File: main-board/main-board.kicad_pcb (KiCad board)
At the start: 2 copper layers, 26 parts, among them IC1 ATMEGA328-A, IC2 FT232RL, J1 INTERFACE1, J2 INTERFACE3, J3 INTERFACE5, J4 INTERFACE5, J5 INTERFACE2, J6 INTERFACE4, J7 INTERFACE6, J8 INTERFACE6, P1 USB_B, P2 CONN_01X02, Y1 Crystal

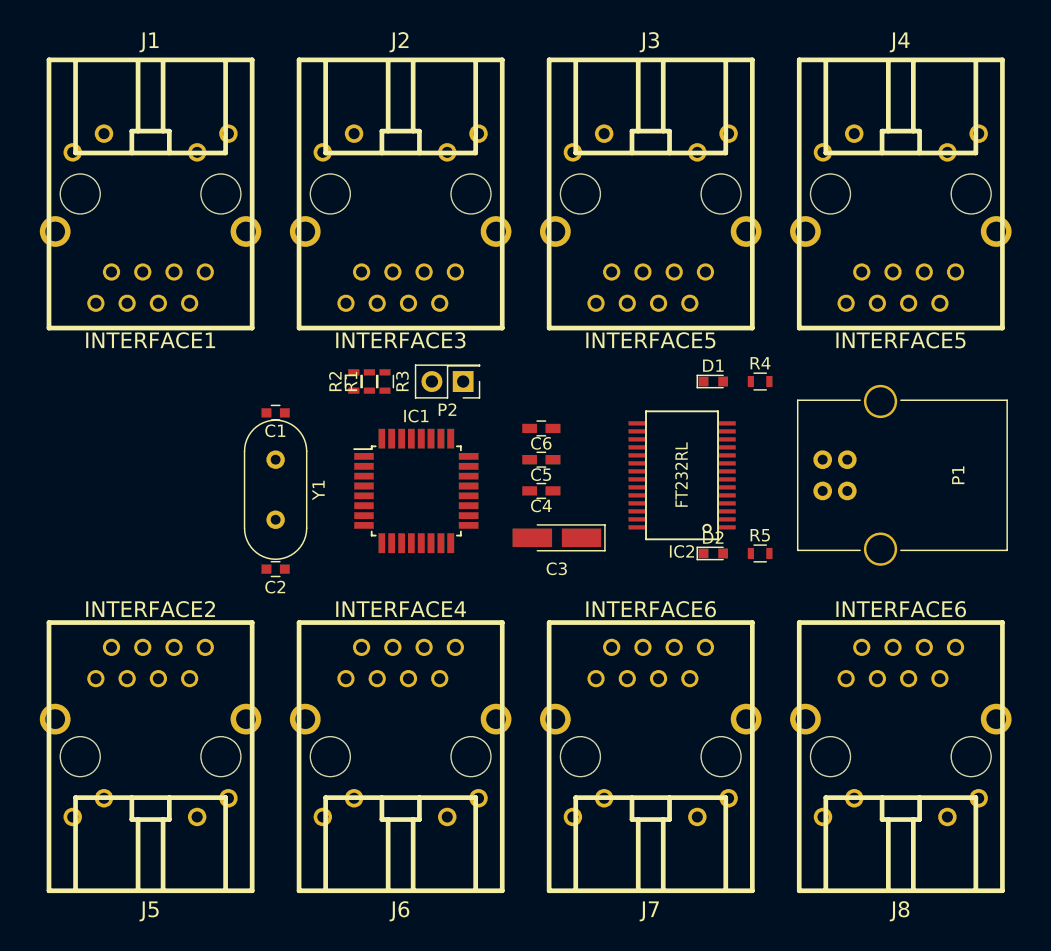
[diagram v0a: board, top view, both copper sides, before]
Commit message: finidhed routing the main-board
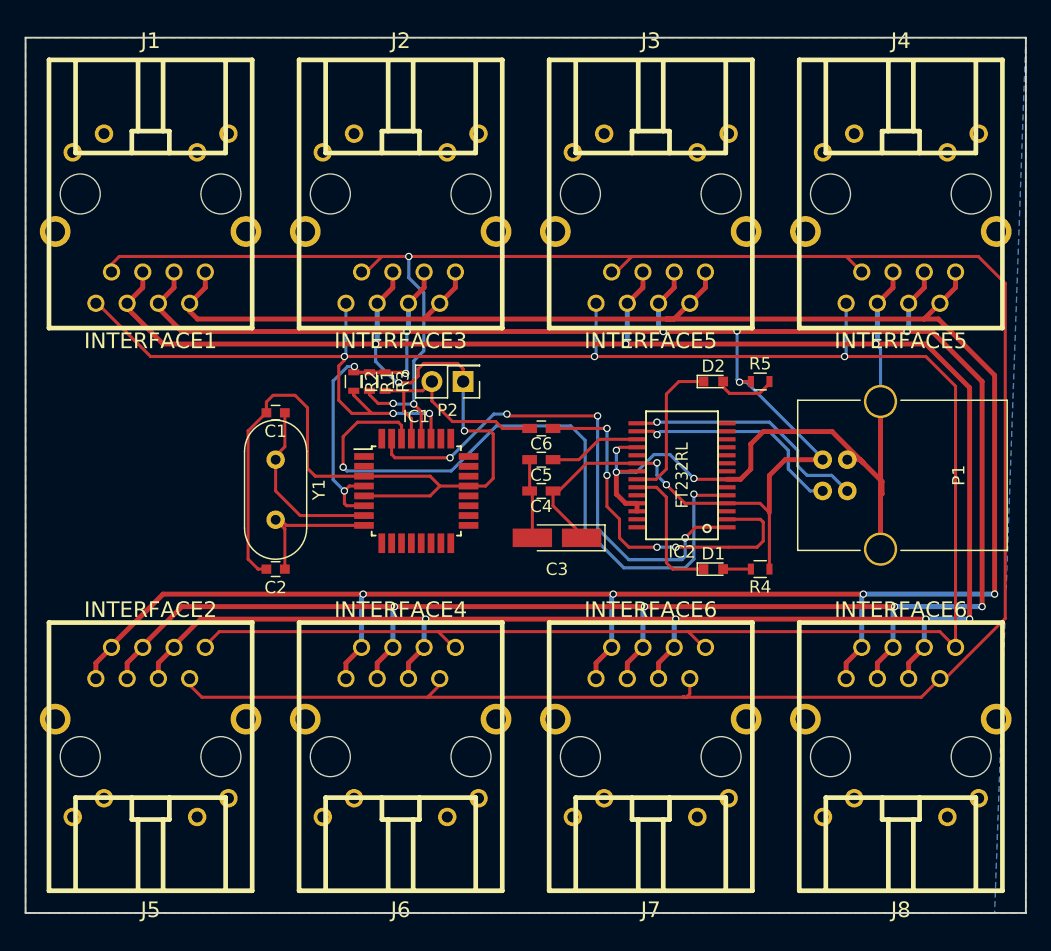
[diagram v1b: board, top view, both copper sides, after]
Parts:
- moved D1 15.2 mm to (124.5, 68.6)
- moved R4 15.2 mm to (128.3, 68.6), turned to 180 degrees
- moved D2 14.0 mm to (124.5, 53.3)
- moved R5 14.0 mm to (128.3, 53.3)
- turned R1 to 270 degrees
- turned R2 to 270 degrees
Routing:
- net GND: track 0.00 -> 322.3 mm, vias 0 -> 12
- net +5V: track 0.00 -> 277.8 mm, vias 0 -> 14
- net +12V: track 0.00 -> 203.3 mm, vias 0 -> 4
- net SCL: track 0.00 -> 201.6 mm, vias 0 -> 3
- net SDA: track 0.00 -> 189.5 mm, vias 0 -> 5
- net RX1: track 0.00 -> 56.3 mm, vias 0 -> 2
- net TX1: track 0.00 -> 42.4 mm, vias 0 -> 4
- net DTR: track 0.00 -> 30.5 mm, vias 0 -> 4
- net Net-(IC2-Pad15): track 0.00 -> 20.2 mm, vias 0 -> 1
- net RST: track 0.00 -> 18.7 mm
- net Net-(IC2-Pad16): track 0.00 -> 18.2 mm, vias 0 -> 1
- net XTAL1: track 0.00 -> 14.7 mm
- net Net-(D2-Pad1): track 0.00 -> 12.3 mm
- net XTAL2: track 0.00 -> 11.7 mm
- net Net-(D1-Pad1): track 0.00 -> 11.3 mm
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- added copper zone on B.Cu, net GND
- added copper zone on F.Cu, net GND
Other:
- board outline added: 81.3 x 71.1 mm

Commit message: final commit with proper silkscreen and pdf exports
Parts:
- renumbered J1 to ?, J2 to ?, J3 to ?, J4 to ?, J5 to ?, J6 to ?, J7 to ?, J8 to ?
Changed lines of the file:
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@@
     (links 108)
     (no_connects 0)
-    (area 68.504999 25.324999 149.935001 96.595001)
+    (area 68.504999 23.93 149.935001 97.6852)
     (thickness 1.6)
     (drawings 4)
@@
     (pad_to_mask_clearance 0.2)
     (aux_axis_origin 0 0)
-    (visible_elements FFFFFF7F)
+    (visible_elements 7FFFFFFF)
     (pcbplotparams
       (layerselection 0x00030_80000001)
@@
       (psnegative false)
       (psa4output false)
-      (plotreference true)
-      (plotvalue true)
+      (plotreference false)
+      (plotvalue false)
       (plotinvisibletext false)
       (padsonsilk false)
@@
       (outputformat 1)
       (mirror false)
-      (drillshape 1)
+      (drillshape 0)
       (scaleselection 1)
-      (outputdirectory ""))
+      (outputdirectory gerbers/))
   )
   (net 0 "")
@@
     (at 78.74 38.1 180)
     (descr "RJ45 + led indicators, Wiznet P/N RB1-125BAG1A")
-    (fp_text reference J1 (at 0 12.446 180) (layer F.SilkS)
+    (fp_text reference "" (at 0 12.446 180) (layer F.SilkS)
       (effects (font (thickness 0.3048)))
     )
@@
     (at 99.06 38.1 180)
     (descr "RJ45 + led indicators, Wiznet P/N RB1-125BAG1A")
-    (fp_text reference J2 (at 0 12.446 180) (layer F.SilkS)
+    (fp_text reference "" (at 0 12.446 180) (layer F.SilkS)
       (effects (font (thickness 0.3048)))
     )
@@
     (at 119.38 38.1 180)
     (descr "RJ45 + led indicators, Wiznet P/N RB1-125BAG1A")
-    (fp_text reference J3 (at 0 12.446 180) (layer F.SilkS)
+    (fp_text reference "" (at 0 12.446 180) (layer F.SilkS)
       (effects (font (thickness 0.3048)))
     )
@@
     (at 139.7 38.1 180)
     (descr "RJ45 + led indicators, Wiznet P/N RB1-125BAG1A")
-    (fp_text reference J4 (at 0 12.446 180) (layer F.SilkS)
+    (fp_text reference "" (at 0 12.446 180) (layer F.SilkS)
       (effects (font (thickness 0.3048)))
     )
@@
     (at 78.74 83.82)
     (descr "RJ45 + led indicators, Wiznet P/N RB1-125BAG1A")
-    (fp_text reference J5 (at 0 12.446) (layer F.SilkS)
+    (fp_text reference "" (at 0 12.446) (layer F.SilkS)
       (effects (font (thickness 0.3048)))
     )
@@
     (at 99.06 83.82)
     (descr "RJ45 + led indicators, Wiznet P/N RB1-125BAG1A")
-    (fp_text reference J6 (at 0 12.446) (layer F.SilkS)
+    (fp_text reference "" (at 0 12.446) (layer F.SilkS)
       (effects (font (thickness 0.3048)))
     )
@@
     (at 119.38 83.82)
     (descr "RJ45 + led indicators, Wiznet P/N RB1-125BAG1A")
-    (fp_text reference J7 (at 0 12.446) (layer F.SilkS)
+    (fp_text reference "" (at 0 12.446) (layer F.SilkS)
       (effects (font (thickness 0.3048)))
     )
@@
     (at 139.7 83.82)
     (descr "RJ45 + led indicators, Wiznet P/N RB1-125BAG1A")
-    (fp_text reference J8 (at 0 12.446) (layer F.SilkS)
-      (effects (font (thickness 0.3048)))
-    )
+    (fp_text reference "" (at 0 12.446) (layer F.SilkS)
+      (effects (font (thickness 0.3048)))
+    )

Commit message: Add branding
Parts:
- added G***: LOGO, custom:logomark.soldermask, F.Cu at (78.1, 64.1)
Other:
- board text added: "design by sudharshan"

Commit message: finished fixes for the board
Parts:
- removed G***: LOGO, custom:logomark.soldermask
- added ?: , EdiCopter:PAD1X6, B.Cu at (148.0, 59.1)
- added ?: , Connectors_Molex:Molex_NanoFit_1x03x2.50mm_Straight, F.Cu at (71.8, 66.7)
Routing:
- net MISO: track 0.00 -> 65.1 mm, vias 0 -> 1
- net GND: track 322.3 -> 378.2 mm
- net RST: track 18.7 -> 73.9 mm, vias 0 -> 3
- net SCK: track 0.00 -> 53.0 mm, vias 0 -> 5
- net MOSI: track 0.00 -> 52.6 mm, vias 0 -> 5
- net +5V: track 277.8 -> 306.4 mm
- net +12V: track 203.3 -> 213.2 mm
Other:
- board text added: "power"

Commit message: Update gerbers and branding
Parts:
- added G***: LOGO, custom:logomark.soldermask, B.Cu at (87.6, 52.7)
